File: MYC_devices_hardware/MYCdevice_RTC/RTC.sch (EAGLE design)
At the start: 30 parts, among them IC1 MEGA8-P, IC2 7805T, Q1 20MHz, X1 8-15V, X2 1503_09, X3 1503_09

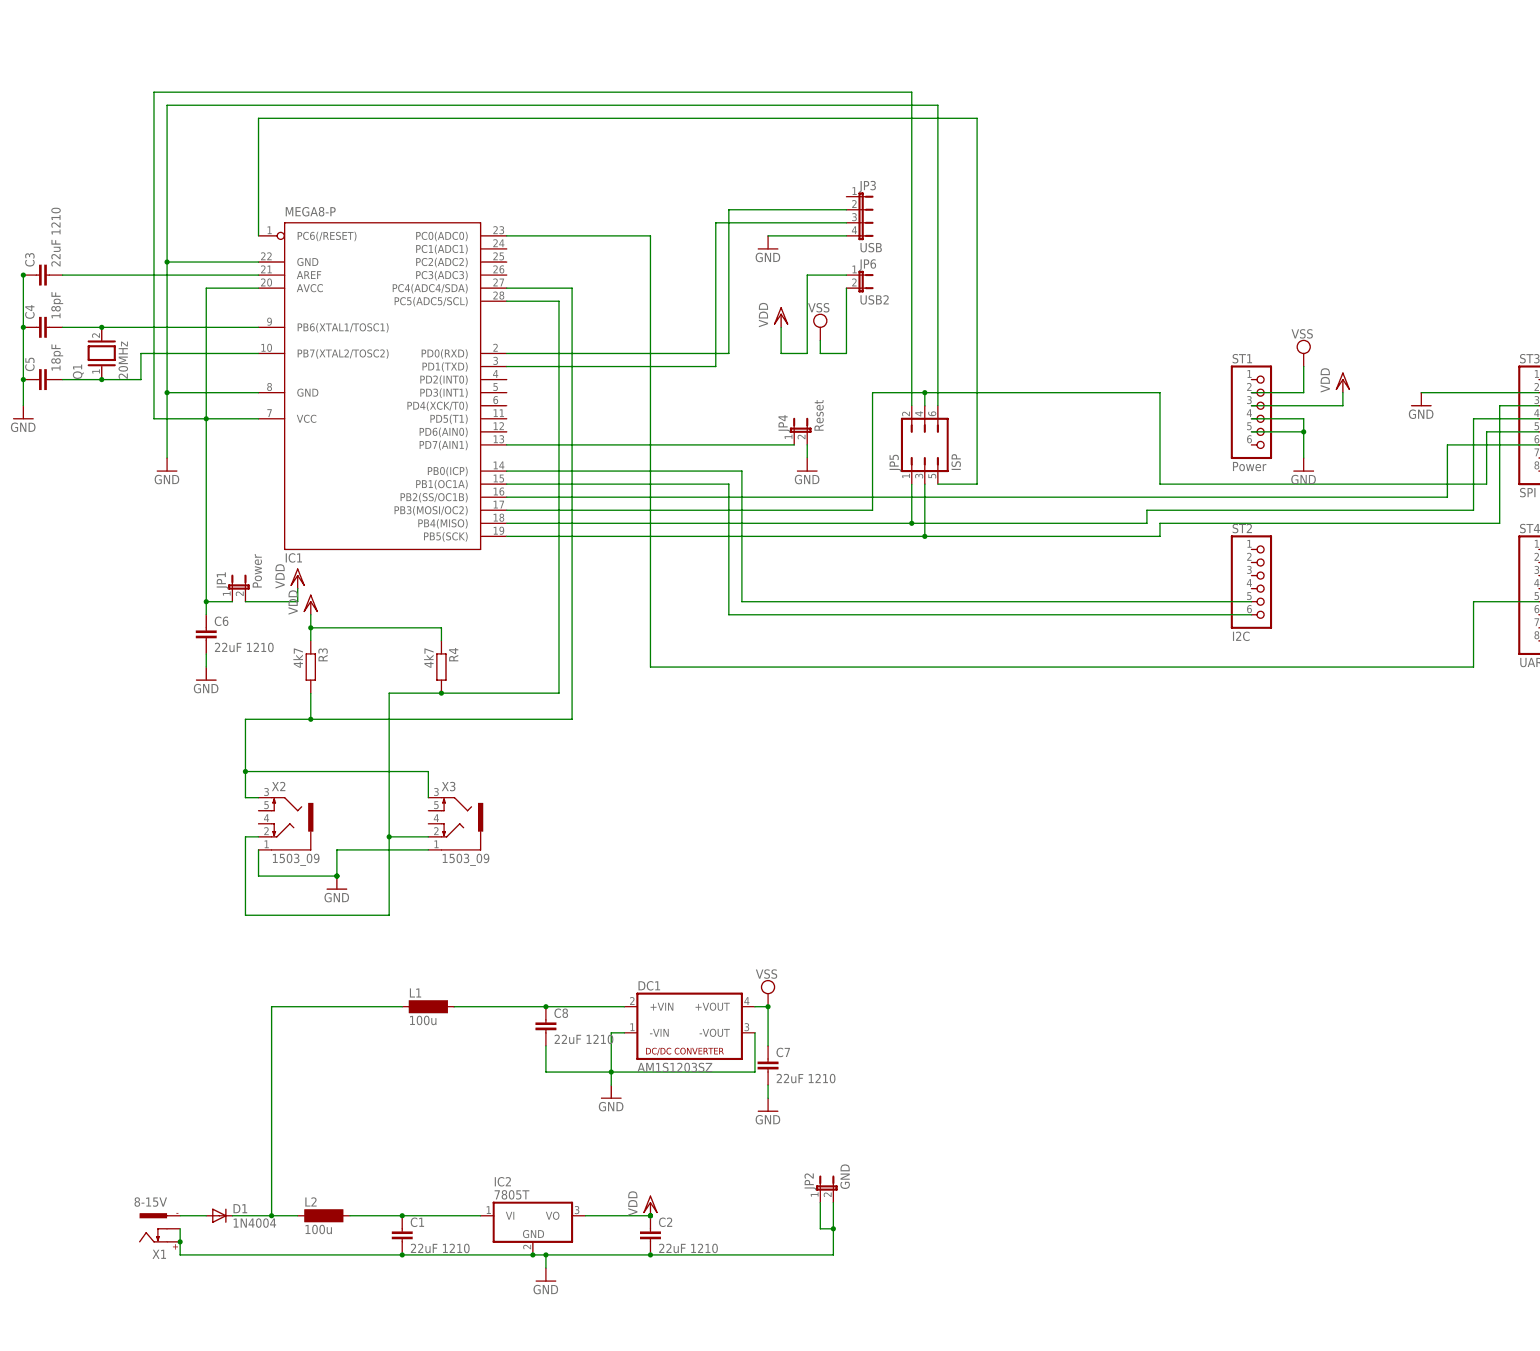
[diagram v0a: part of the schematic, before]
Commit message: board with RS232, bascom with includes
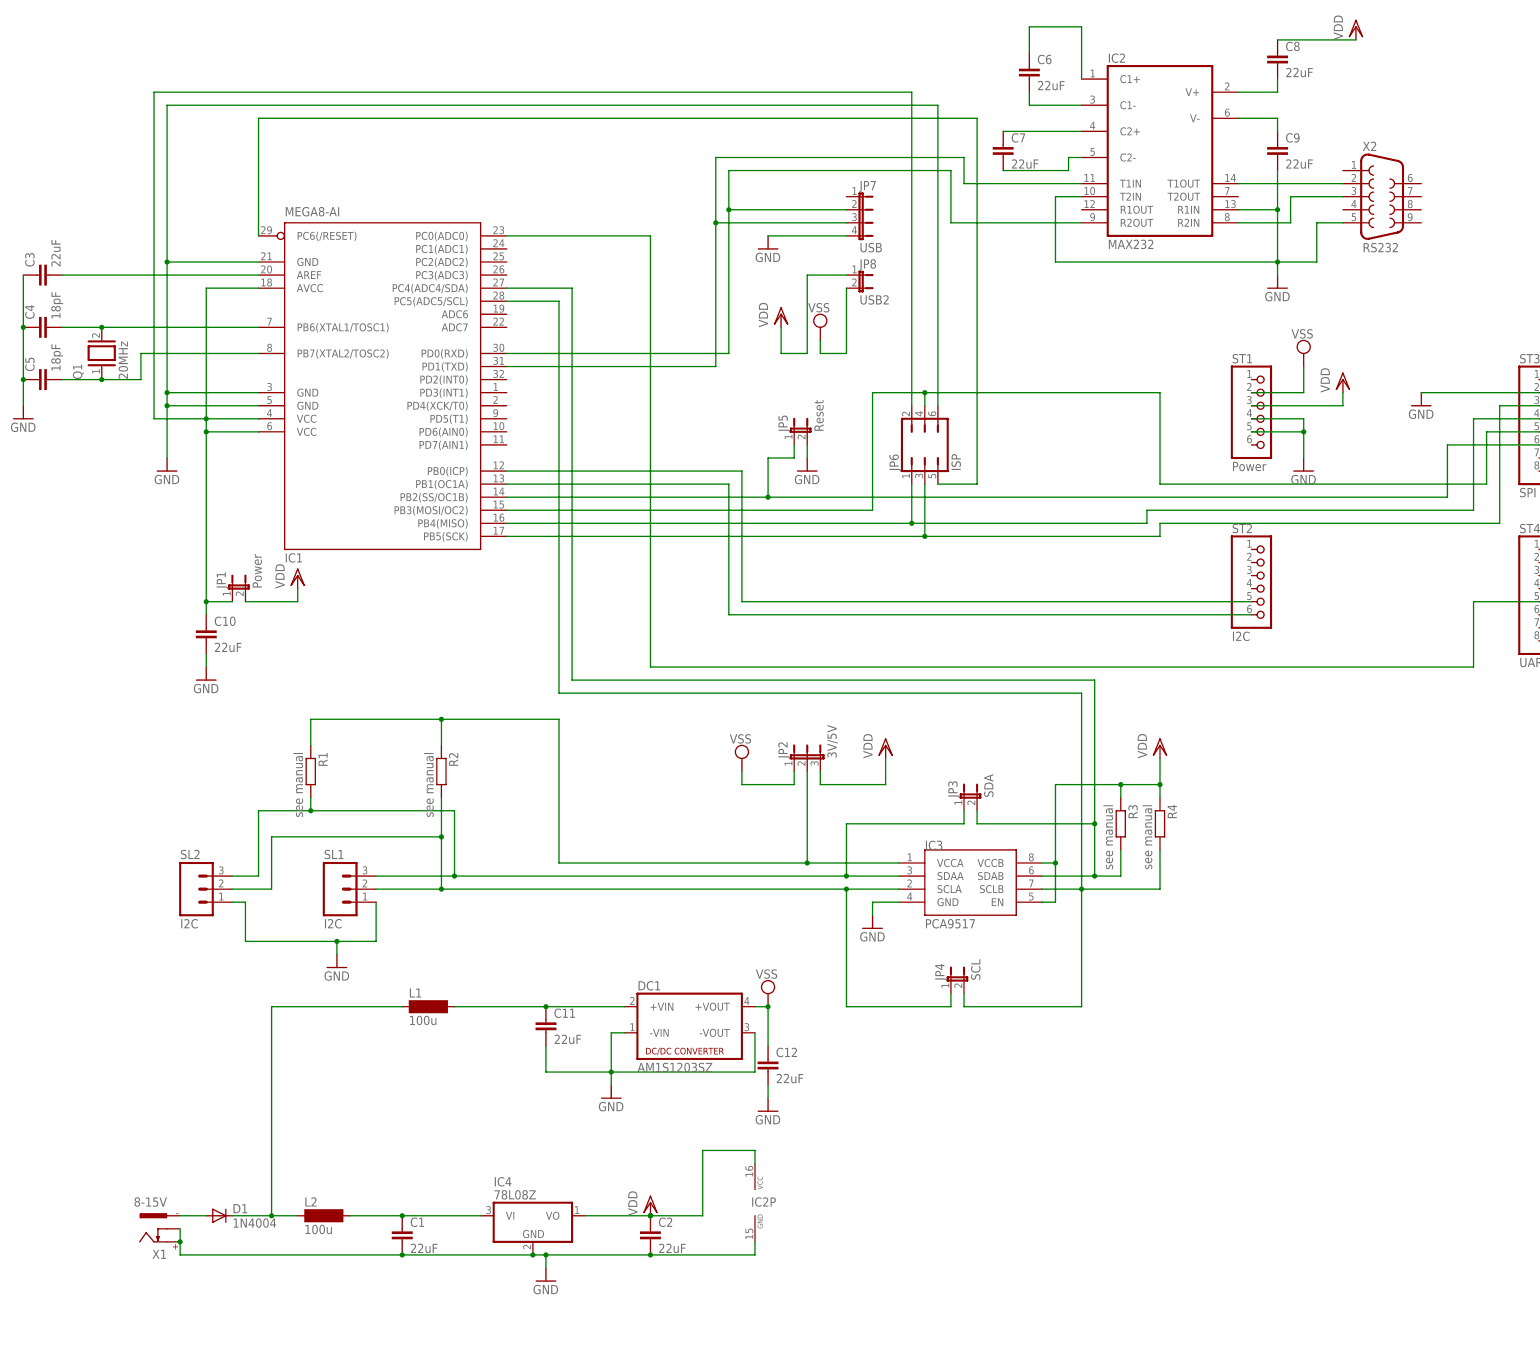
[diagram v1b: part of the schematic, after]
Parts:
- removed X3: 1503_09, con-lumberg:1503_09
- added C10, C11, C12, C9: 22uF, rcl:C-EUC1206
- added IC3: PCA9517, PCA9517:PCA9517
- added IC4: 78L08Z, linear:78L08Z
- added JP7: USB, jumper:JP4E
- added JP8: USB2, jumper:JP1E
- added R1, R2: see manual, resistor:R-EU_R1206
- added SL1, SL2: I2C, con-amp-quick:M03
- C1, C2, C3, C6, C7, C8: value 22uF 1210 -> 22uF
- IC1: value MEGA8-P -> MEGA8-AI; device atmel:MEGA8-P -> atmel:MEGA8-AI
- IC2: value 7805T -> MAX232; device linear:7805T -> maxim:MAX232
- JP2: value GND -> 3V/5V; device jumper:JP1E -> jumper:JP2E
- JP3: value USB -> SDA; device jumper:JP4E -> jumper:JP1E
- JP4: value Reset -> SCL
- JP5: value ISP -> Reset; device jumper:JP3Q -> jumper:JP1E
- JP6: value USB2 -> ISP; device jumper:JP1E -> jumper:JP3Q
- R3, R4: value 4k7 -> see manual
- X2: value 1503_09 -> RS232; device con-lumberg:1503_09 -> con-subd:F09H
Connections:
- new net N$11: IC3.SCLA, JP4.1, R2.2, SL1.2, SL2.2
- new net N$12: IC3.SDAA, JP3.1, R1.2, SL1.3, SL2.3
- new net N$13: IC2G$1.T1OUT, X2.2
- new net N$14: C8.2, IC2G$1.V+
- new net N$16: C9.1, IC2G$1.V-
- new net N$21: IC3.VCCA, JP2.2, R1.1, R2.1
- new net N$23: C6.1, IC2G$1.C1+
- new net N$24: C6.2, IC2G$1.C1-
- new net N$25: C7.1, IC2G$1.C2+
- new net N$26: C7.2, IC2G$1.C2-
- net GND: now also C10.2, C11.2, C12.2, C9.2, IC1.GND@2, IC2G$1.R1IN, IC2G$1.T2IN, IC2P.GND, IC3.GND, IC4.GND, JP5.2, JP6.6, JP7.4, SL1.1, SL2.1, X2.5; no longer C6.2, C7.2, C8.2, IC2.GND, JP2.1, JP2.2, JP3.4, JP4.2, JP5.6, X2.1, X3.1
- net N$15: now also JP6.1; no longer JP5.1
- net N$18: now also JP6.5; no longer JP5.5
- net N$20: now also JP6.3; no longer JP5.3
- net N$22: now also IC3.SCLB, JP4.2; no longer X2.2, X3.2
- net N$28: now also JP6.4; no longer JP5.4
- net N$3: now also C11.1; no longer C8.1
- net N$33: now also IC4.VI; no longer IC2.VI
- net N$4: now also JP5.1
- net N$44: now also C10.1, IC1.VCC@2, JP6.2; no longer C6.1, JP5.2
- net N$5: now also IC3.SDAB, JP3.2; no longer X2.3, X3.3
- net N$6: now also IC2G$1.R2IN, X2.3; no longer IC1.PD7(AIN1), JP4.1
- net N$8: now also IC2G$1.T1IN, JP7.3; no longer JP3.3
- net N$9: now also IC2G$1.R2OUT, JP7.2; no longer JP3.2
- net VDD: now also C8.1, IC2P.VCC, IC3.EN, IC3.VCCB, IC4.VO, JP2.3, JP8.1; no longer IC2.VO, JP6.1
- net VSS: now also C12.1, JP2.1, JP8.2; no longer C7.1, JP6.2
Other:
- moved on the sheet: C6, C7, C8, JP4, R3, R4
